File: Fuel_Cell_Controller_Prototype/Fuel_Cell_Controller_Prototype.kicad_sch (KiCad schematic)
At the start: 6 parts

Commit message: update
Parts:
- added C28: 10u, symbol Device:C
- added C29: C_Polarized_Small_US, symbol Device:C_Polarized_Small_US
- added R4, R6, R7, R8: 100k, symbol Device:R
- added R5: R_US, symbol Device:R_US
- added U3, U4: LTC6269, Package_SO:MSOP-8-1EP_3x3mm_P0.65mm_EP1.68x1.88mm, symbol FCCParts:LTC6269
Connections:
- net +12V: now also U3.8 (V+)
- new net: U3.1 (OUTA), U3.2 (-INA)
- new net: U3.6 (-INB), U3.7 (OUTB)
- new net GND: U3.4 (V-), U3.9 (V-_Pad)
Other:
- sheet Microcontroller ports: added PG0; removed none

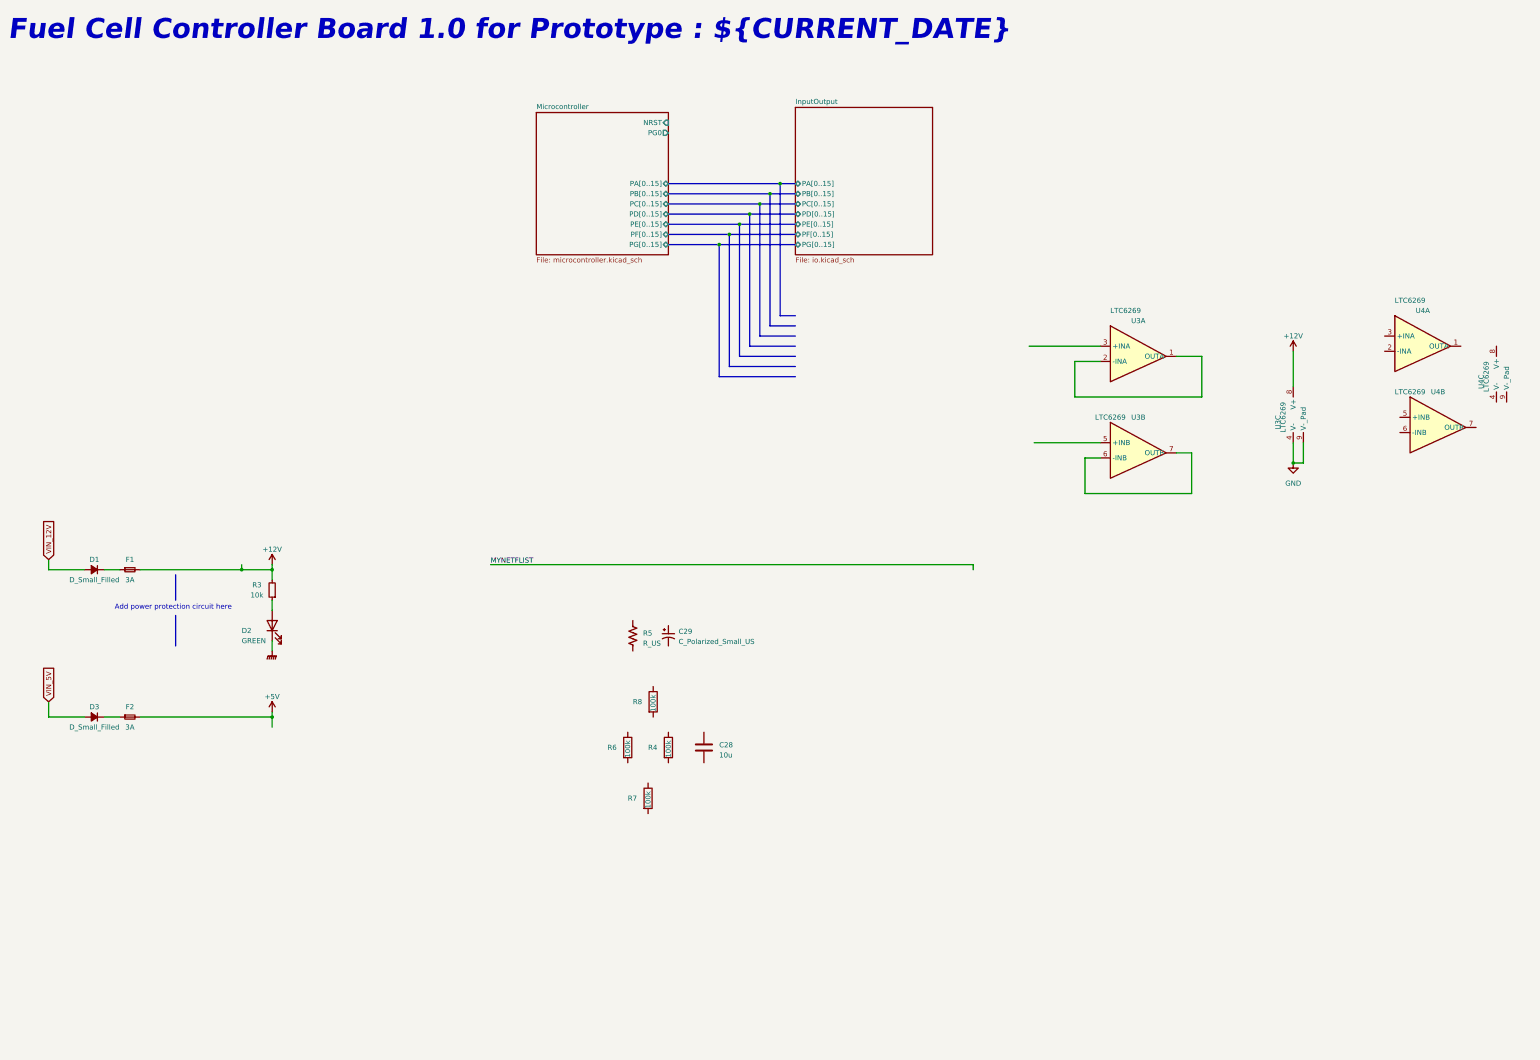
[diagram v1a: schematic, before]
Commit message: Added 6POS Molex connectors and started implementation of eFuses for 12v and 5V protection
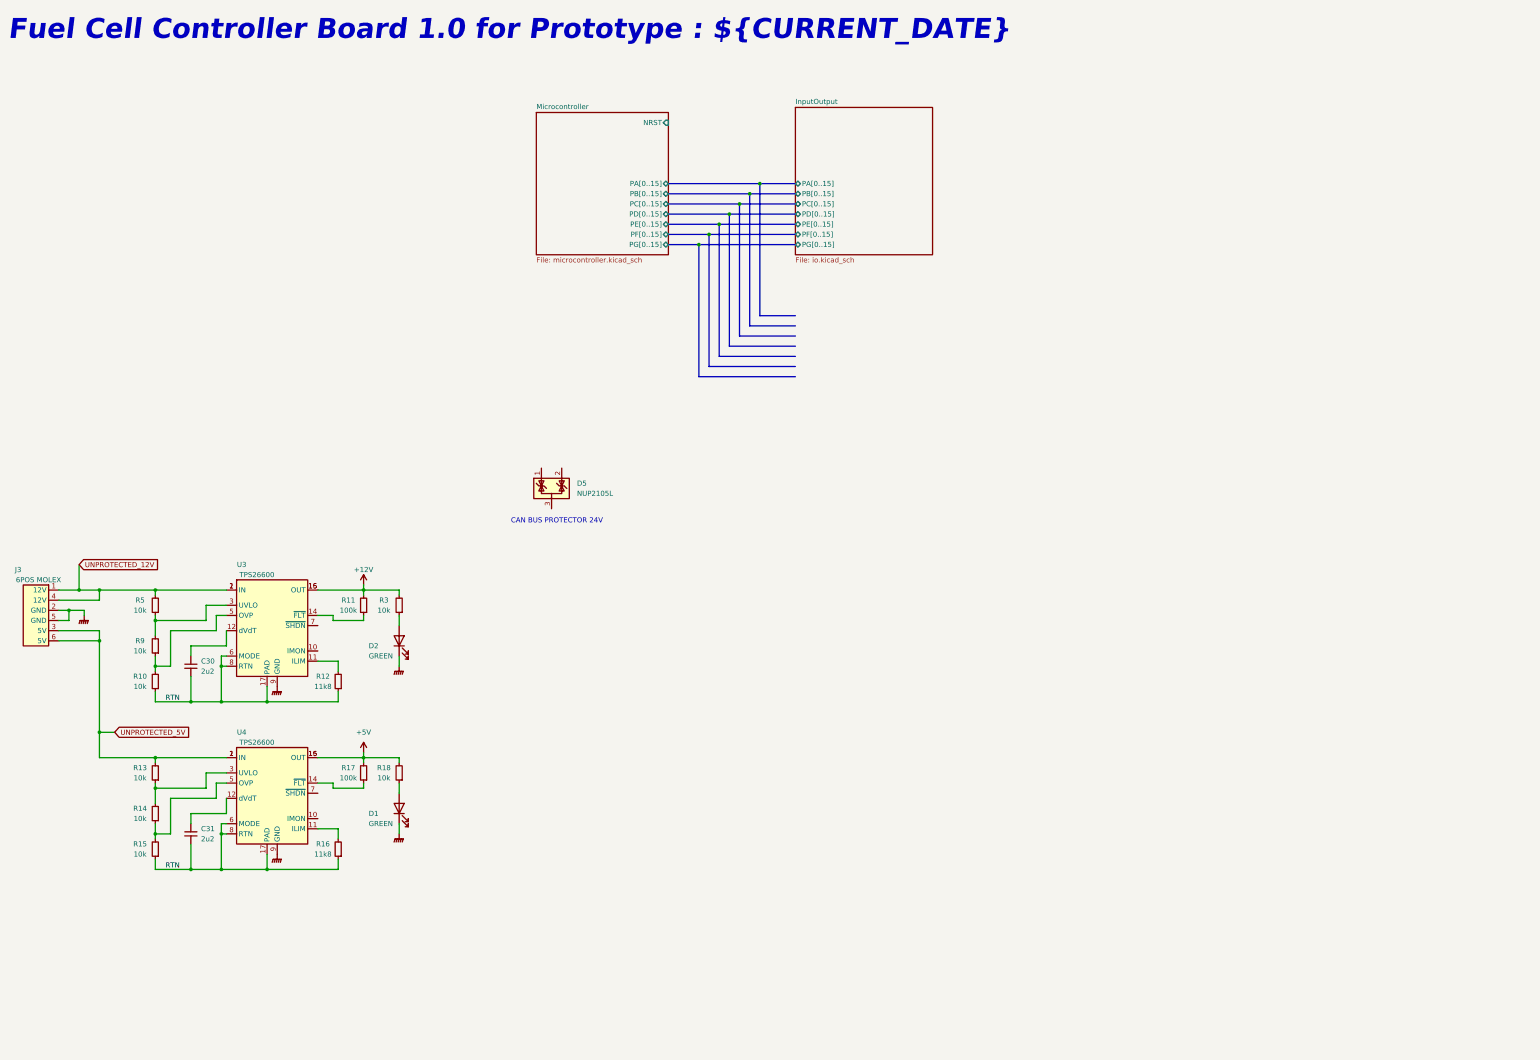
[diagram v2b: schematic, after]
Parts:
- removed C28: 10u, symbol Device:C
- removed C29: C_Polarized_Small_US, symbol Device:C_Polarized_Small_US
- removed D1, D3: D_Small_Filled, symbol Device:D_Small_Filled
- removed F1, F2: 3A, symbol Device:Fuse_Small
- removed R4, R6, R7, R8: 100k, symbol Device:R
- removed R5: R_US, symbol Device:R_US
- removed U3, U4: LTC6269, Package_SO:MSOP-8-1EP_3x3mm_P0.65mm_EP1.68x1.88mm, symbol FCCParts:LTC6269
- added C30, C31: 2u2, symbol Device:C_Small
- added D1: GREEN, symbol Device:LED
- added D5: NUP2105L, Package_TO_SOT_SMD:SOT-23, symbol Power_Protection:NUP2105L
- added J3: 6POS MOLEX, Connector_Molex:Molex_Micro-Fit_3.0_43045-0612_2x03_P3.00mm_Vertical, symbol FCC_Parts:MOLEX_6POS
- added R10, R13, R14, R15, R18, R5, R9: 10k, symbol Device:R_Small
- added R11, R17: 100k, symbol Device:R_Small
- added R12, R16: 11k8, symbol Device:R_Small
- added U3, U4: TPS26600, symbol FCC_Parts:TPS26600
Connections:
- net +12V: now also R11.2, U3.15 (OUT), U3.16 (OUT)
- net +5V: now also R17.2, R18.2, U4.15 (OUT), U4.16 (OUT)
- net GNDPWR: now also D1.1 (K), J3.2 (GND), J3.5 (GND), U3.9 (GND), U4.9 (GND)
- new net: R13.1, R14.2, U4.3 (UVLO)
- new net: R12.2, U3.11 (ILIM)
- new net: C30.1, U3.12 (dVdT)
- new net: U3.13 (NC), U3.4 (NC)
- new net: R11.1, U3.14 (~{FLT})
- new net: R5.1, R9.2, U3.3 (UVLO)
- new net: R10.2, R9.1, U3.5 (OVP)
- new net: R14.1, R15.2, U4.5 (OVP)
- new net: R16.2, U4.11 (ILIM)
- new net: C31.1, U4.12 (dVdT)
- new net: U4.13 (NC), U4.4 (NC)
- new net: R17.1, U4.14 (~{FLT})
- new net: D1.2 (A), R18.1
- new net RTN: C30.2, C31.2, R10.1, R12.1, R15.1, R16.1, U3.17 (PAD), U3.6 (MODE), U3.8 (RTN), U4.17 (PAD), U4.6 (MODE), U4.8 (RTN)
- new net UNPROTECTED_12V: J3.1 (12V), J3.4 (12V), R5.2, U3.1 (IN), U3.2 (IN)
- new net UNPROTECTED_5V: J3.3 (5V), J3.6 (5V), R13.2, U4.1 (IN), U4.2 (IN)
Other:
- sheet Microcontroller ports: added none; removed PG0
- note added: "CAN BUS PROTECTOR 24V"
- note removed: "Add power protection circuit here"
- moved on the sheet: D2, R3

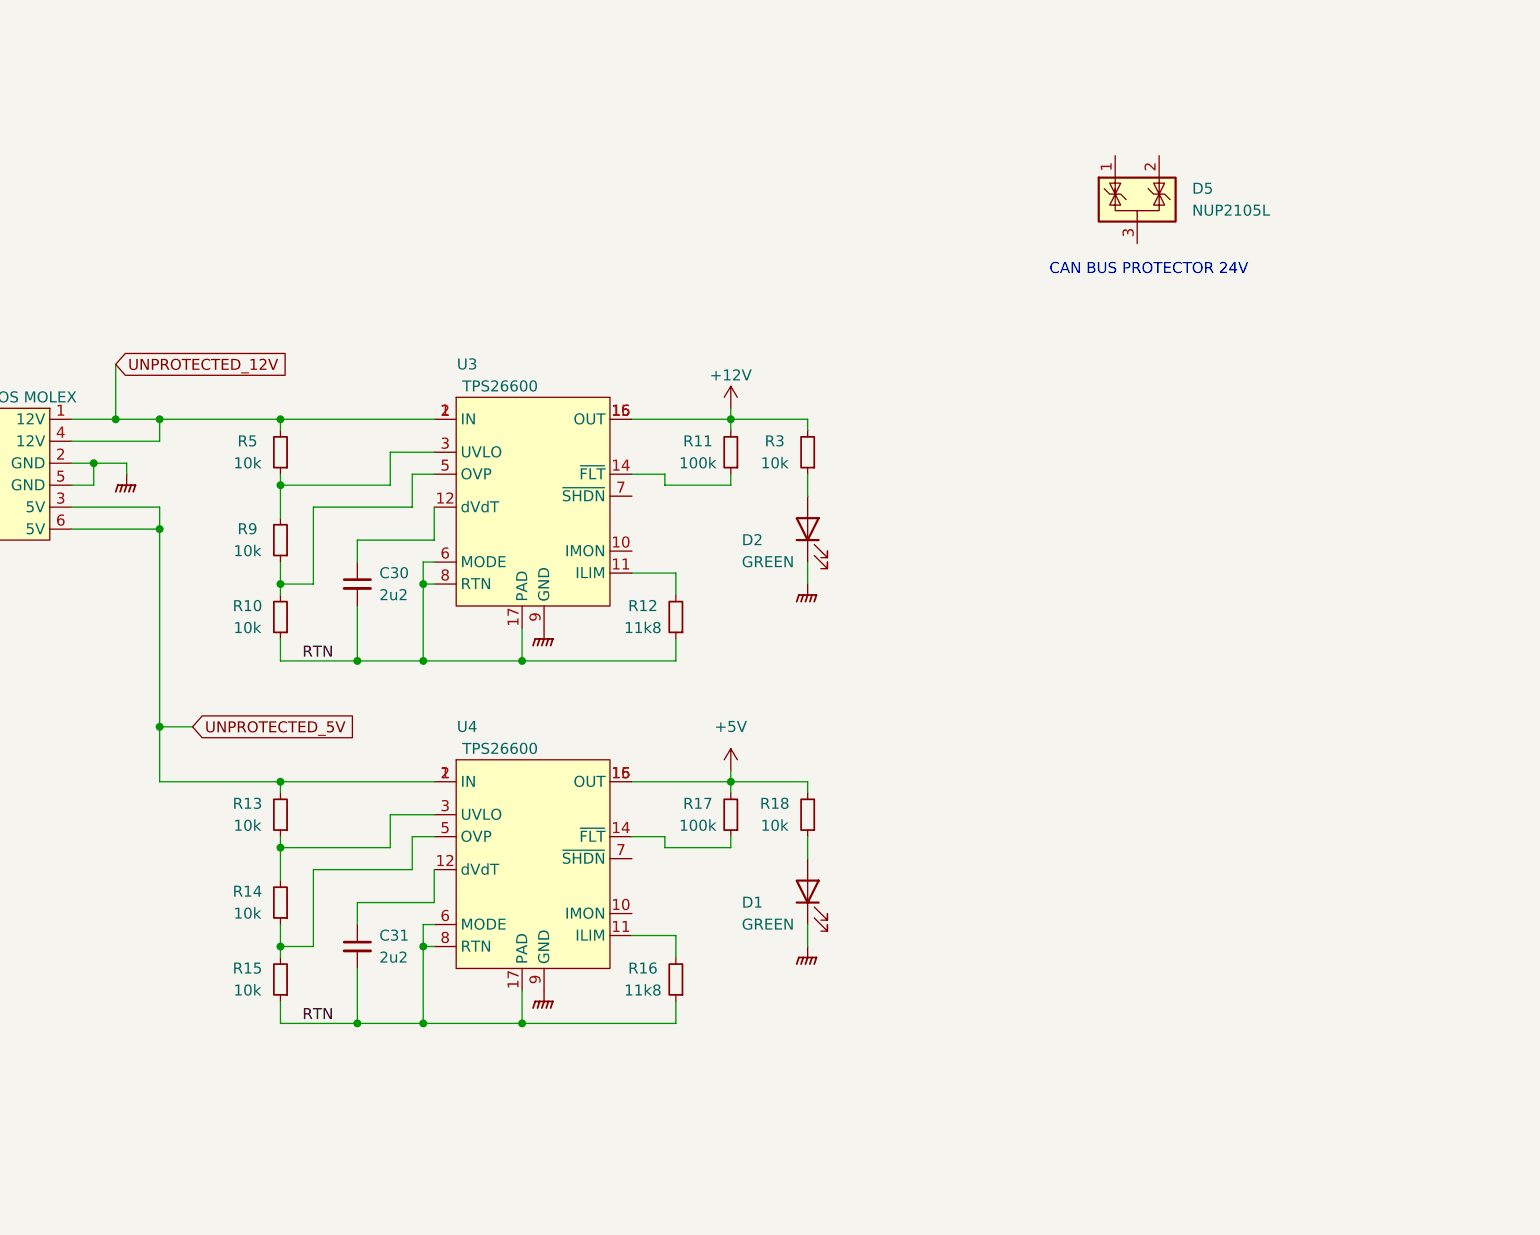
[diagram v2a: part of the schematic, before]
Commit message: Added actual eFuses with parts that can be bought. Some work still needs to be done with the MOSFETS for the leds
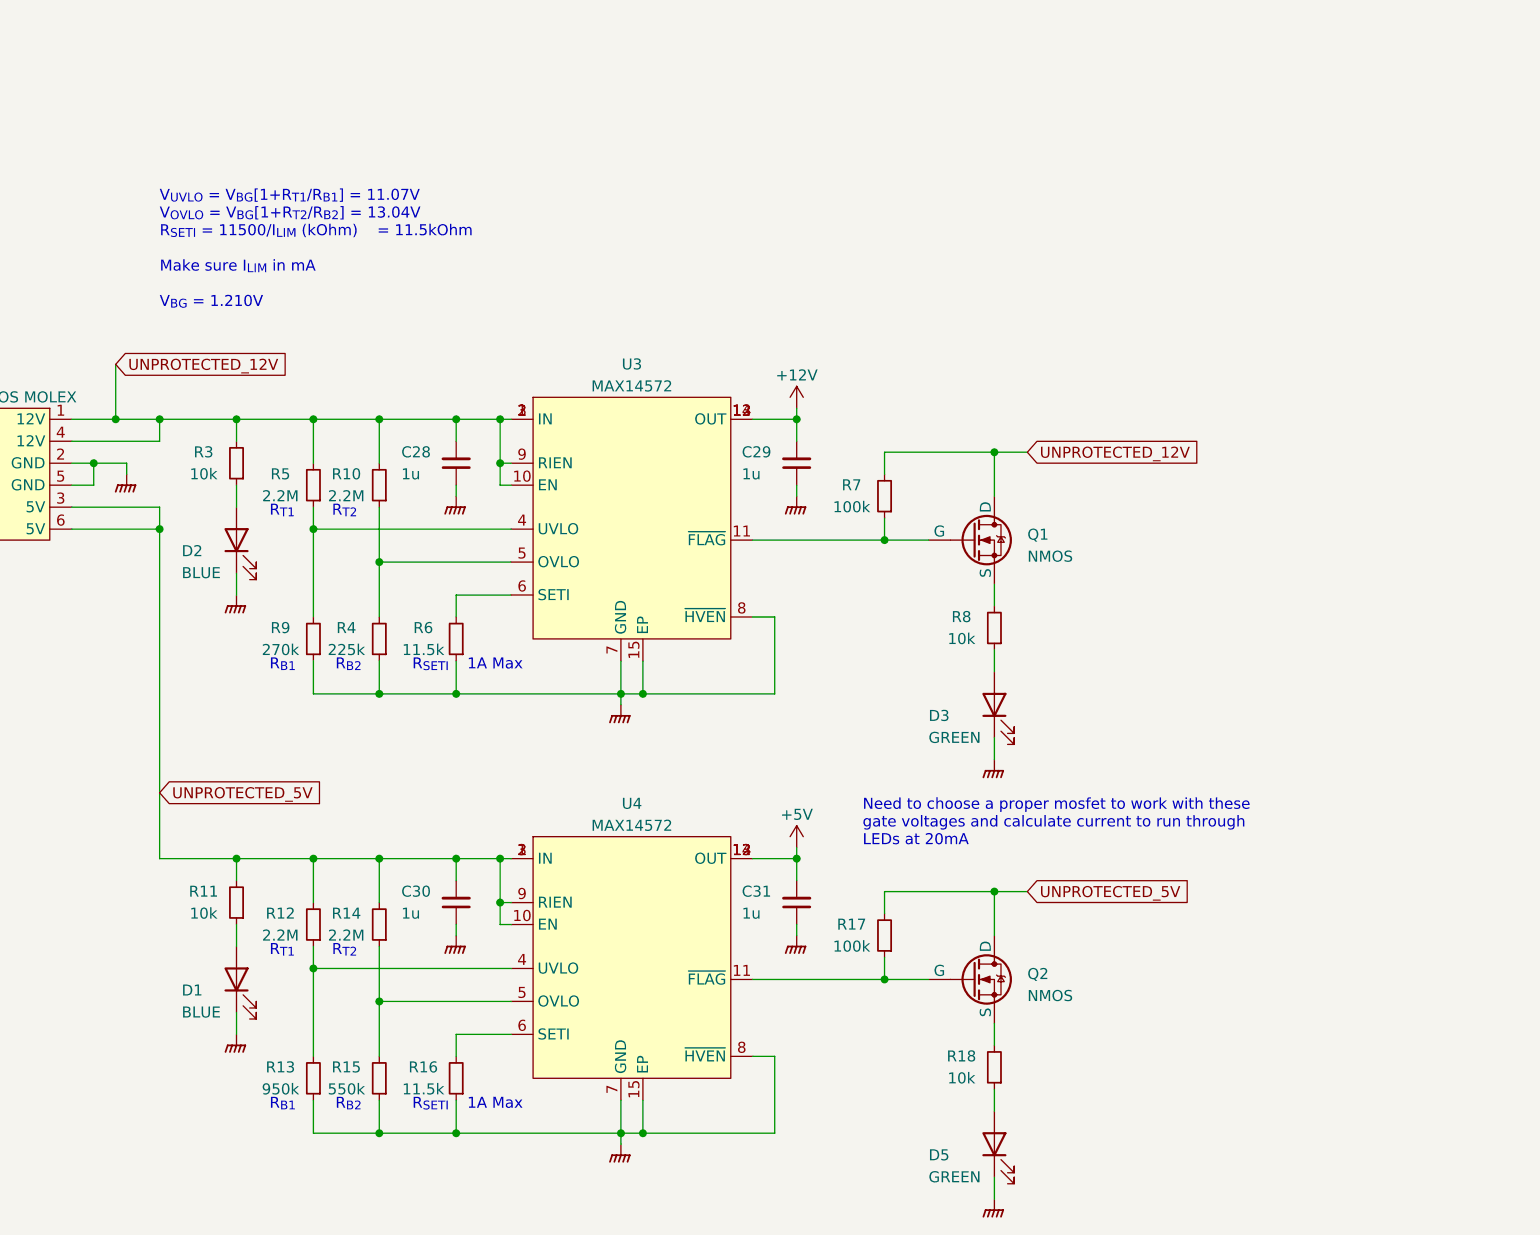
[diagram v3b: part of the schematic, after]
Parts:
- removed D5: NUP2105L, Package_TO_SOT_SMD:SOT-23, symbol Power_Protection:NUP2105L
- removed U3, U4: TPS26600, symbol FCC_Parts:TPS26600
- added C28, C29: 1u, symbol Device:C_Small
- added D3, D5: GREEN, symbol Device:LED
- added Q1, Q2: NMOS, symbol Simulation_SPICE:NMOS
- added R4: 225k, symbol Device:R_Small
- added R6: 11.5k, symbol Device:R_Small
- added R7: 100k, symbol Device:R_Small
- added R8: 10k, symbol Device:R_Small
- added U3, U4: MAX14572, Package_SO:TSSOP-14-1EP_4.4x5mm_P0.65mm, symbol FCC_Parts:MAX14572
- C30, C31: value 2u2 -> 1u
- D1, D2: value GREEN -> BLUE
- R10, R14, R5: value 10k -> 2.2M
- R11: value 100k -> 10k
- R12: value 11k8 -> 2.2M
- R13: value 10k -> 950k
- R15: value 10k -> 550k
- R16: value 11k8 -> 11.5k
- R9: value 10k -> 270k
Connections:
- net +12V: now also C29.2, U3.12 (OUT), U3.13 (OUT), U3.14 (OUT); no longer R11.2, R3.2
- net +5V: now also C31.2, U4.12 (OUT), U4.13 (OUT), U4.14 (OUT); no longer R17.2, R18.2
- net GNDPWR: now also C30.1, C31.1, R13.1, R15.1, R16.1, R9.1, C28.1, C29.1, D3.1 (K), D5.1 (K), R4.1, R6.1, U3.15 (EP), U3.7 (GND), U3.8 (~{HVEN}), U4.15 (EP), U4.7 (GND), U4.8 (~{HVEN})
- net UNPROTECTED_12V: now also R10.2, R3.2, C28.2, Q1.1 (D), R7.2, U3.1 (IN), U3.10 (EN), U3.2 (IN), U3.3 (IN), U3.9 (RIEN)
- net UNPROTECTED_5V: now also C30.2, R11.2, R12.2, R14.2, R17.2, Q2.1 (D), U4.1 (IN), U4.10 (EN), U4.2 (IN), U4.3 (IN), U4.9 (RIEN); no longer R13.2
- net at R11.1: now also D1.2 (A)
- net at R5.1, R9.2: now also U3.4 (UVLO)
- net at R14.1, R15.2: now also U4.5 (OVLO)
- net at R16.2: now also U4.6 (SETI)
- net at R17.1: now also Q2.2 (G), U4.11 (~{FLAG})
- net at R18.1: now also D5.2 (A); no longer D1.2 (A)
- removed net RTN: C30.2, C31.2, R10.1, R12.1, R15.1, R16.1
- new net: R12.1, R13.2, U4.4 (UVLO)
- new net: D3.2 (A), R8.1
- new net: Q2.3 (S), R18.2
- new net: Q1.2 (G), R7.1, U3.11 (~{FLAG})
- new net: R10.1, R4.2, U3.5 (OVLO)
- new net: R6.2, U3.6 (SETI)
- new net: Q1.3 (S), R8.2
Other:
- note added: "1A Max"
- note added: "Need to choose a proper mosfet to work with these gate voltages and calculate current to run through LEDs at 20mA"
- note added: "R_{B1}"
- note added: "R_{B2}"
- note added: "R_{SETI}"
- note added: "R_{T1}"
- note added: "R_{T2}"
- note added: "V_{UVLO} = V_{BG}[1+R_{T1}/R_{B1}] = 11.07V V_{OVLO} = V_{BG}[1+R_{T2}/R_{B2}] = 13.04V R_{SETI} = 11500/I_{LIM} (kOhm) = 11.5kOhm Make sure I_{LIM} in mA V_{BG} = 1.210V"
- note removed: "CAN BUS PROTECTOR 24V"
- moved on the sheet: D2, R10, R3, R5, R9

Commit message: Updates
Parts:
- added C33: 10, symbol Device:C
- added D6, D8: BZV55C3V3, Diode_SMD:D_MiniMELF, symbol Diode:BZV55C3V3
- added R21, R22, R23, R24: 10k, symbol Device:R
- added R25: 1k, symbol Device:R
- added R26: 2k, symbol Device:R
- added R27: 9.1k, symbol Device:R
- added R28: 3.6k, symbol Device:R
- added U6: SHT31-DIS, Sensor_Humidity:Sensirion_DFN-8-1EP_2.5x2.5mm_P0.5mm_EP1.1x1.7mm, symbol Sensor_Humidity:SHT31-DIS
- added U7, U8: BUF602xD, Package_SO:SOIC-8_3.9x4.9mm_P1.27mm, symbol Amplifier_Buffer:BUF602xD
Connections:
- net +12V: now also R27.1
- net +5V: now also R25.1
- new net: R27.2, R28.1, U7.4 (IN)
- new net: R21.2, U6.1 (SDA)
- new net: R25.2, R26.1, U8.4 (IN)
- new net: R24.1, U6.6 (~{RESET})
- new net: R23.2, U6.2 (ADDR)
- new net: R22.2, U6.4 (SCL)
- new net 12V_Ref: D8.1 (K), U7.8
- new net 5V_Ref: D6.1 (K), U8.8
- new net GND: C33.2, D6.2 (A), D8.2 (A), R23.1, R26.2, R28.2, U6.7 (R), U6.8 (VSS), U6.9 (VSS)
- new net VDD: C33.1, R21.1, R22.1, R24.2, U6.5 (VDD)
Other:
- note added: "Adafruit SCH31"
- note added: "R_{1}"
- note added: "R_{2}"
- note added: "V_{in} = V_{s}[R_{2}/R_{1}+R_{2}] = 3.3V R_{2} = 0.38R_{1}"
- note added: "V_{in} = V_{s}[R_{2}/R_{1}+R_{2}] = 3.3V R_{2} = 1.94R_{1}"
- company: (none) -> EcoCar
- title: (none) -> Fuel Cell Controller Board

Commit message: Update - Mikael
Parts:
- C33: value 10 -> 100n
- R25: value 1k -> 100k
- R26: value 2k -> 200k
- R27: value 9.1k -> 910k
- R28: value 3.6k -> 360k
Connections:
- net GND: now also U7.5 (V-), U8.5 (V-)
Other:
- note added: "3.3V"
- moved on the sheet: C28, C29, C30, C31, C33, D1, D2, D3, D5, D6, D8, J3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
